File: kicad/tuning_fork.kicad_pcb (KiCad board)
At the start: 2 copper layers, 69.3 x 66 mm, 32 parts, among them J1 AudioIn, J2 TuningFork, J3 OscOut, J4 USB_B_Mini, J5 Conn_Coaxial, J6 Conn_Coaxial, J7 Iout, J8 AudioJack3, SW1 SW_SPDT, SW2 SW_SPDT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

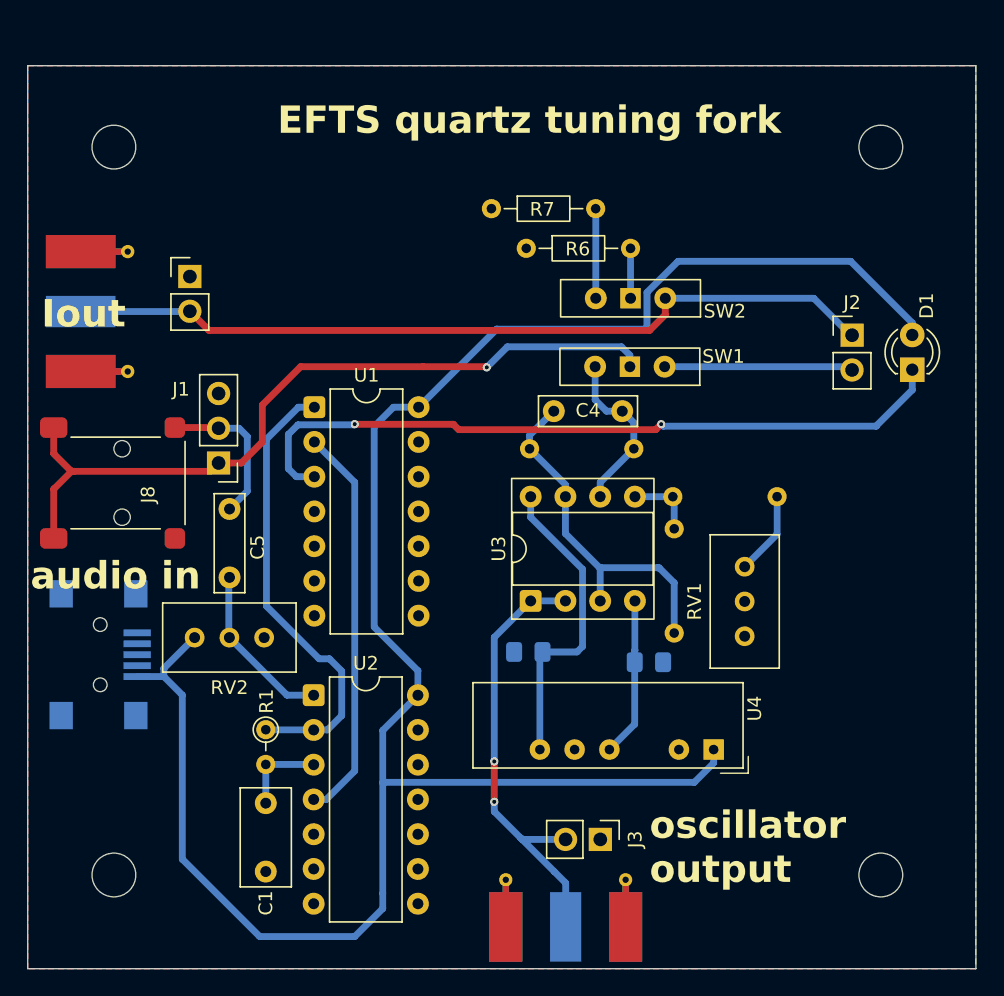
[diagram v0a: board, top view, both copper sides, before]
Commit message: move mounthing holes to RPi5 location
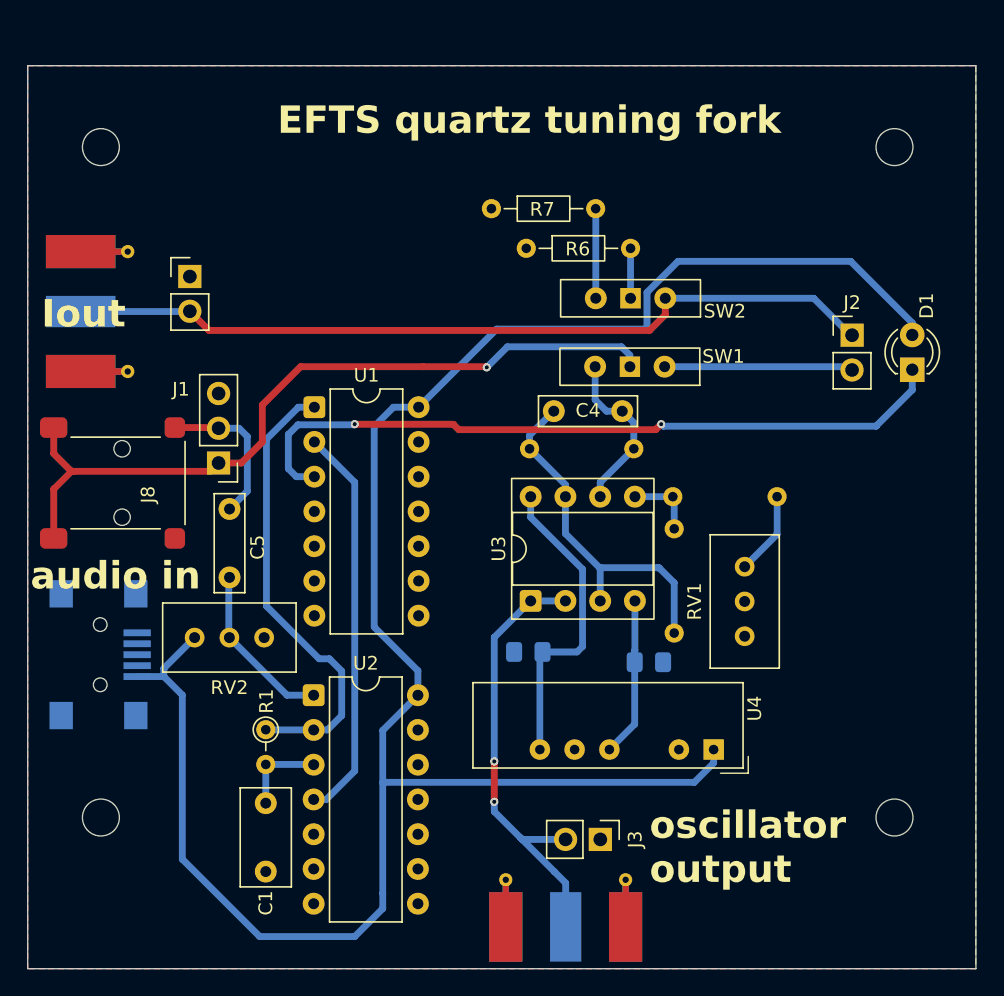
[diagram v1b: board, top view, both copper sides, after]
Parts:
- H1, H2, H3, H4: footprint MountingHole:MountingHole_3.2mm_M3 -> MountingHole:MountingHole_2.7mm_M2.5
- moved H3 4.32 mm to (134.1, 86.0), turned to 90 degrees
- moved H4 4.31 mm to (76.0, 86.0)
- moved H1 1.00 mm to (134.1, 37.0)
- moved H2 0.95 mm to (76.0, 37.0)

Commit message: improved layout for usability
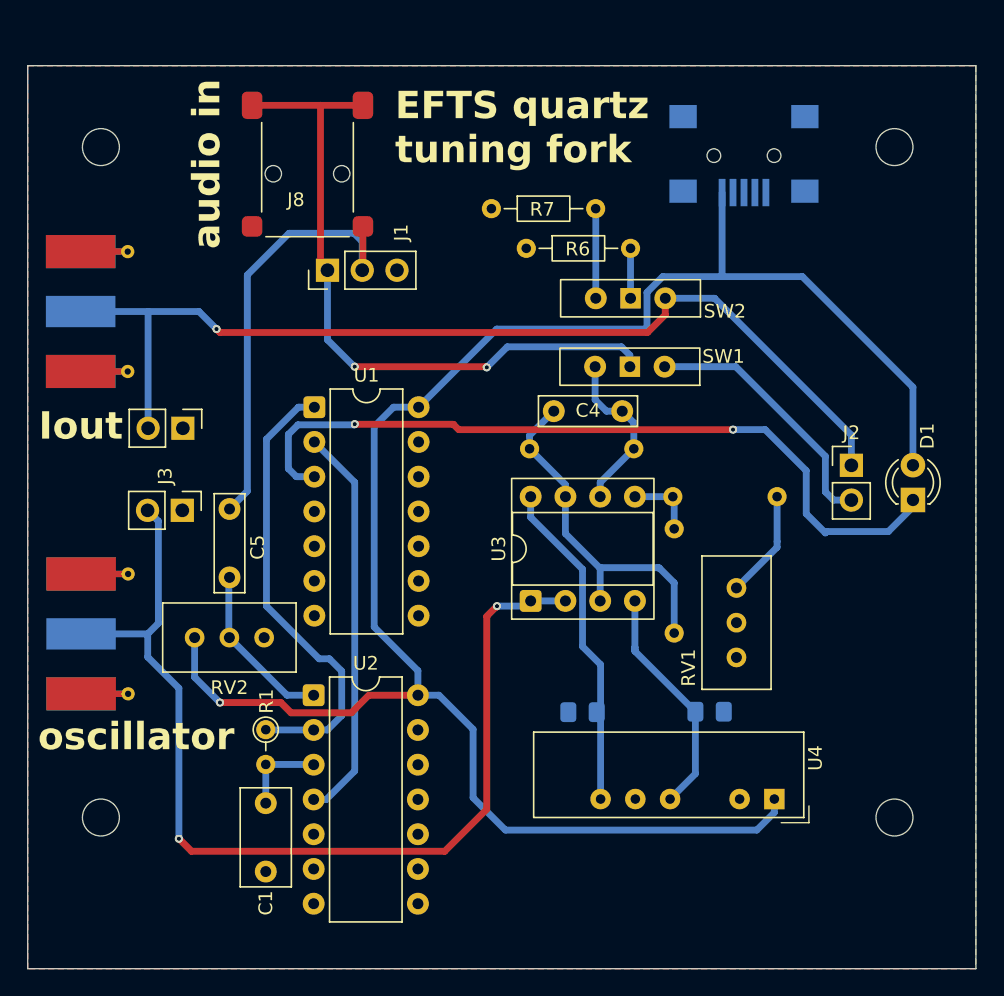
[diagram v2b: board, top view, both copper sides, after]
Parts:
- moved J4 59.5 mm to (123.0, 37.6), turned to 0 degrees
- moved J6 39.0 mm to (76.3, 72.5), turned to 0 degrees
- moved J3 38.9 mm to (82.0, 63.5)
- moved J8 29.8 mm to (91.2, 36.4), turned to 0 degrees
- moved J1 16.2 mm to (92.6, 46.0), turned to 90 degrees
- moved J7 11.1 mm to (82.0, 57.5), turned to -90 degrees
- moved D1 9.52 mm to (135.4, 62.7)
- moved J2 9.51 mm to (130.9, 60.2)
- moved C2 5.92 mm to (111.2, 78.2)
- moved C3 5.73 mm to (120.5, 78.2)
- moved U4 5.73 mm to (125.3, 84.6)
- moved RV1 1.66 mm to (122.5, 69.2)
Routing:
- net Net-(J3-Pin_2): track 33.0 -> 74.9 mm
- net Net-(J1-Pin_2): track 11.4 -> 32.9 mm
- net Net-(J2-Pin_1): track 59.8 -> 73.6 mm, vias 0 -> 1
- net VCC: track 149.5 -> 137.0 mm, vias 0 -> 1
- net Net-(J1-Pin_1): track 56.5 -> 50.1 mm, vias 1 -> 2
- net Net-(U3C-V-): track 11.6 -> 17.3 mm
- net Net-(J2-Pin_2): track 14.2 -> 19.6 mm
- net Net-(D1-K): track 53.5 -> 57.0 mm
- net Net-(R3-Pad1): track 6.10 -> 7.90 mm
- net Net-(U3C-V+): track 22.8 -> 24.2 mm
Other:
- board text added: "oscillator"
- board text removed: "oscillator output"

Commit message: add RPi +5V supply header
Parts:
- added J9: Conn_01x03_Pin, Connector_PinSocket_2.54mm:PinSocket_1x03_P2.54mm_Vertical, B.Cu at (80.9, 35.7)
- RV2: value 1k/10 turns -> 10k/10 turns
- moved J8 4.15 mm to (95.3, 36.4)
- moved J1 2.05 mm to (92.5, 48.0)
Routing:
- net VCC: track 137.0 -> 174.1 mm
- net Net-(J1-Pin_2): track 32.9 -> 38.6 mm

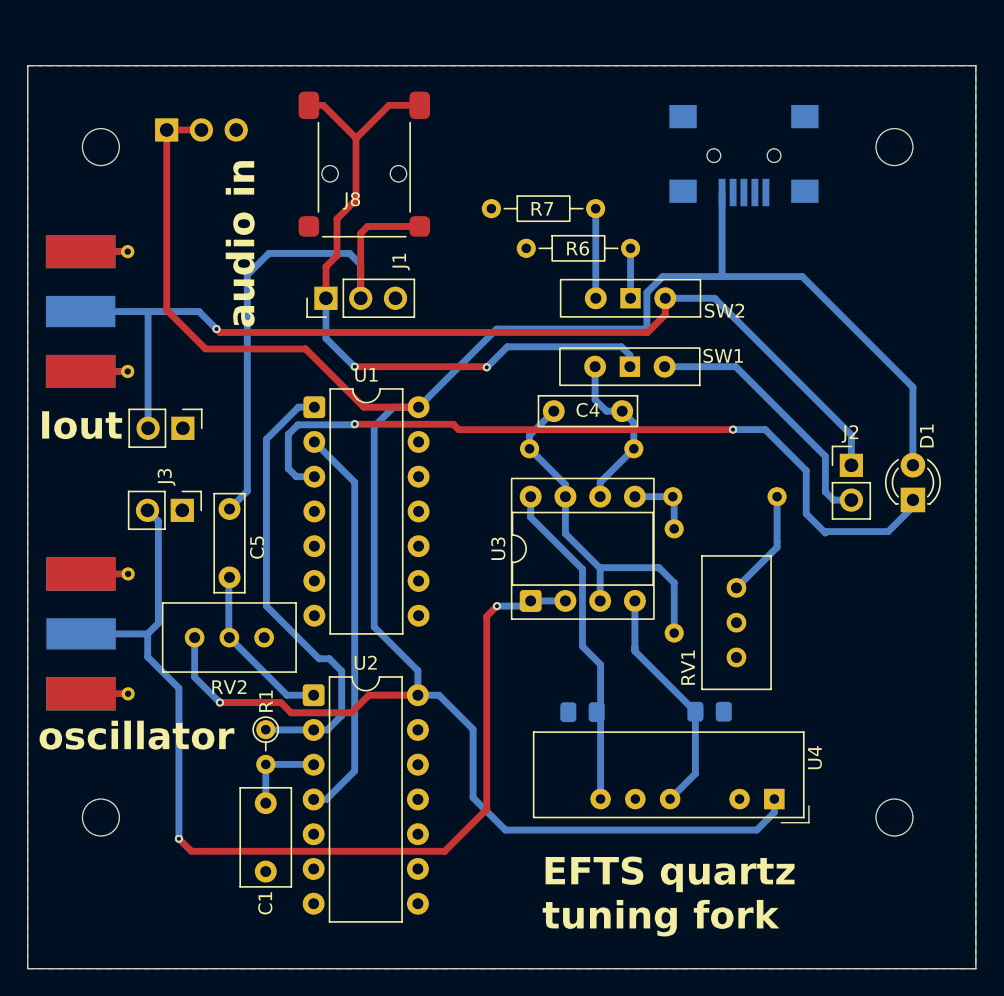
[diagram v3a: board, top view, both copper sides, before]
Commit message: add oscillator reset push button
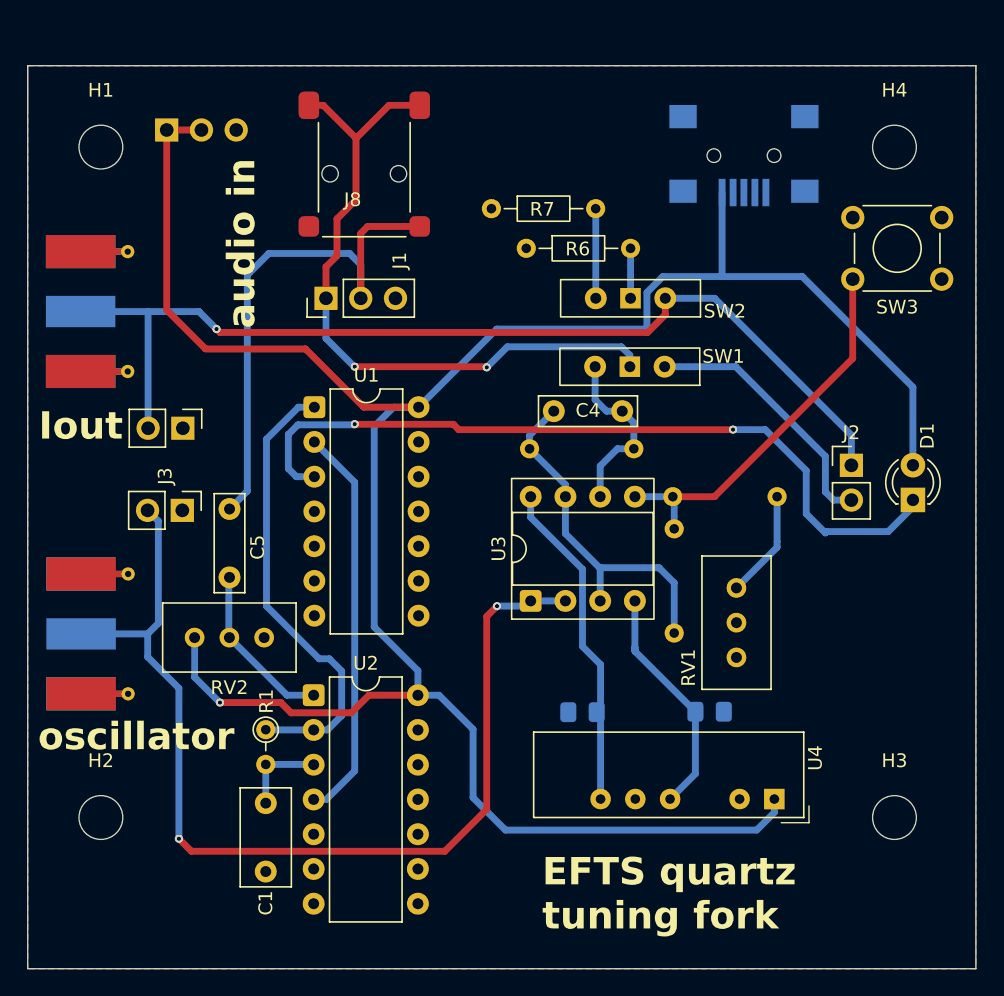
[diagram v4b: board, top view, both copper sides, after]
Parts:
- added SW3: SW_SPST, Button_Switch_THT:SW_TH_Tactile_Omron_B3F-100x, F.Cu at (137.5, 46.6)
- H1, H2, H3, H4: footprint MountingHole:MountingHole_2.7mm_M2.5 -> MountingHole:MountingHole_3.2mm_M3
- moved H4 75.9 mm to (134.1, 37.0)
- moved H1 58.0 mm to (76.0, 37.0)
- moved H2 49.0 mm to (76.0, 86.0)
- turned H3 to 0 degrees
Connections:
- C5 pad 1: Net-(J1-Pin_2) -> Net-(C5-Pad1)
- J1 pad 1: Net-(J1-Pin_1) -> unconnected-(J1-Pin_1-Pad1)
- J1 pad 2: Net-(J1-Pin_2) -> unconnected-(J1-Pin_2-Pad2)
- J8 pad R: Net-(J1-Pin_2) -> Net-(C5-Pad1)
- J8 pad T: Net-(J1-Pin_1) -> Net-(SW1-A)
- SW1 pad 1: Net-(J1-Pin_1) -> Net-(SW1-A)
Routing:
- net (no net): track 0.00 -> 89.1 mm, vias 0 -> 2
- net Net-(J1-Pin_1): track 50.4 -> 0.00 mm, vias 2 -> 0
- net Net-(J1-Pin_2): track 38.6 -> 0.00 mm
- net Net-(SW3-A): track 5.16 -> 28.4 mm
- net Net-(SW1-C): track 12.8 -> 13.5 mm
